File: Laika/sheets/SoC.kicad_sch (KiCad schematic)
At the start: 2 parts, among them J6 Conn_01x03, U1 Milk-V Duo Module

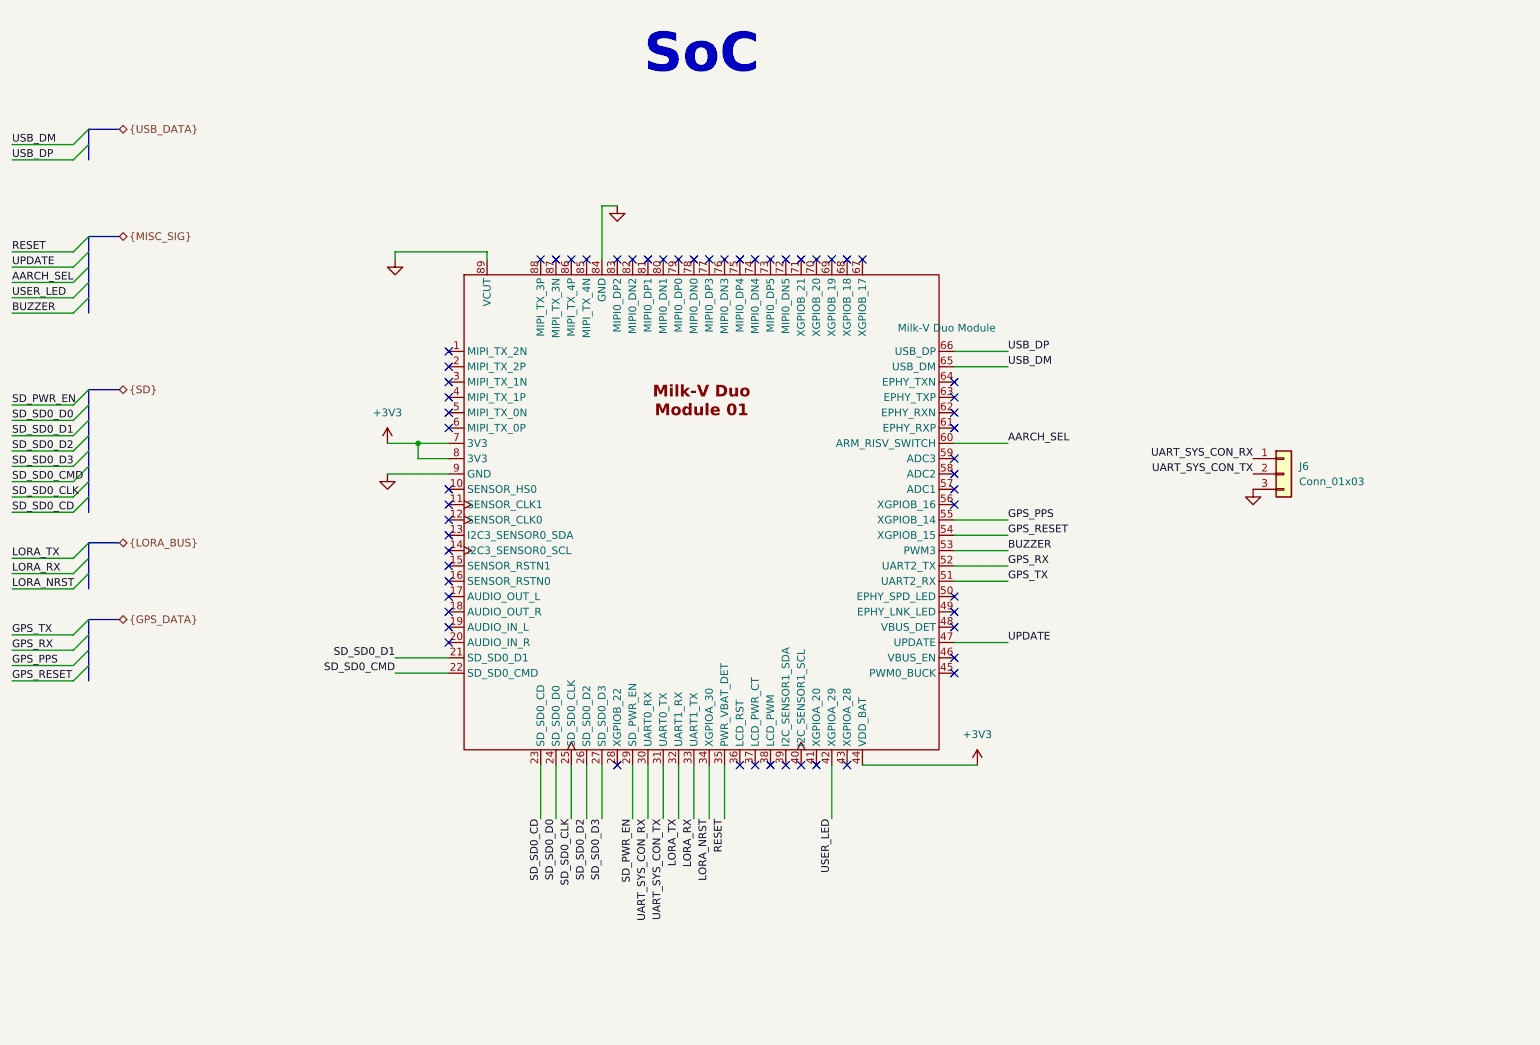
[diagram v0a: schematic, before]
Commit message: Connected sensors to SPI3
Connected Sensor Bus to SPI3. Rearranged GPS reset, pps, and buzzer pins
to other 3.3V logic pins. Connected SPI chip selects. Deleted interrupt
bus from sensors due to lack of 3.3V pins.
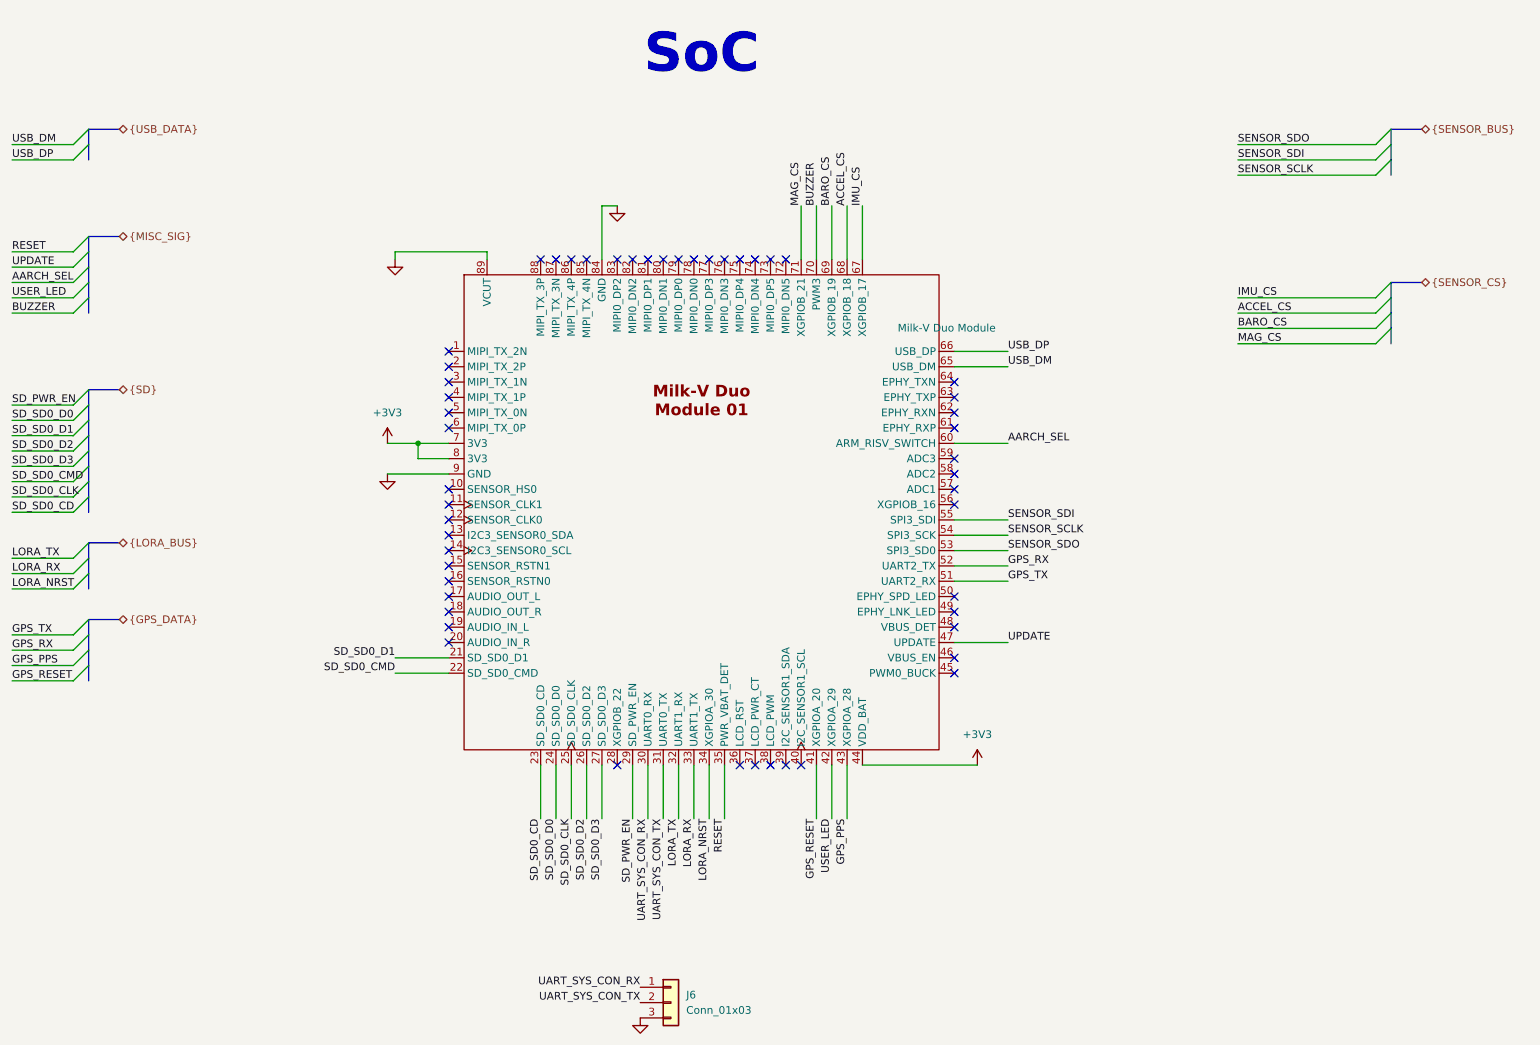
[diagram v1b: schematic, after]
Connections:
- net BUZZER: now also U1.70 (XGPIOB_20); no longer U1.53 (XGPIOB_13)
- net GPS_PPS: now also U1.43 (XGPIOA_28); no longer U1.55 (XGPIOB_14)
- net GPS_RESET: now also U1.41 (XGPIOA_20); no longer U1.54 (XGPIOB_15)
- net IMU_CS: now reaches U1.67 (XGPIOB_17)
- net ACCEL_CS: now reaches U1.68 (XGPIOB_18)
- net BARO_CS: now reaches U1.69 (XGPIOB_19)
- net MAG_CS: now reaches U1.71 (XGPIOB_21)
- new net SENSOR_SCLK: U1.54 (XGPIOB_15)
- new net SENSOR_SDI: U1.55 (XGPIOB_14)
- new net SENSOR_SDO: U1.53 (XGPIOB_13)
- no-connect marks 59 -> 52
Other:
- moved on the sheet: J6
